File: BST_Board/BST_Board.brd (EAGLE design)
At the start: 59.4 x 27.9 mm, 35 parts, among them J1 UP2-AH-1-TH, J4 EMPCB.SMAFSTJ.B.HT, U1 STM32L053C8T6, U2 RFM69HCW, U5 LM3671MF-3.3/NOPB, Y1 ECS-80-S-4X

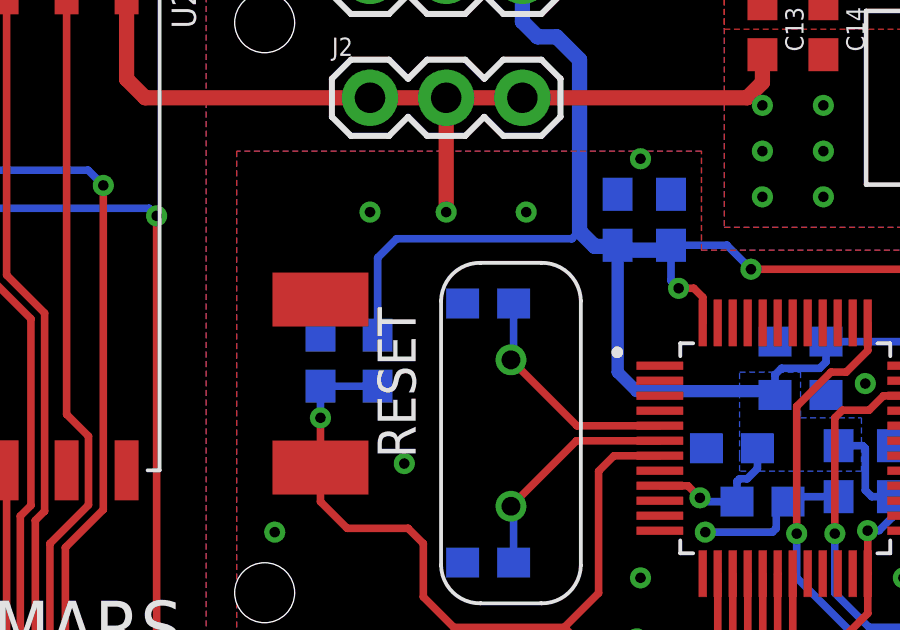
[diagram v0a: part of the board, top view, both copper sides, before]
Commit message: Fixed reset circuit
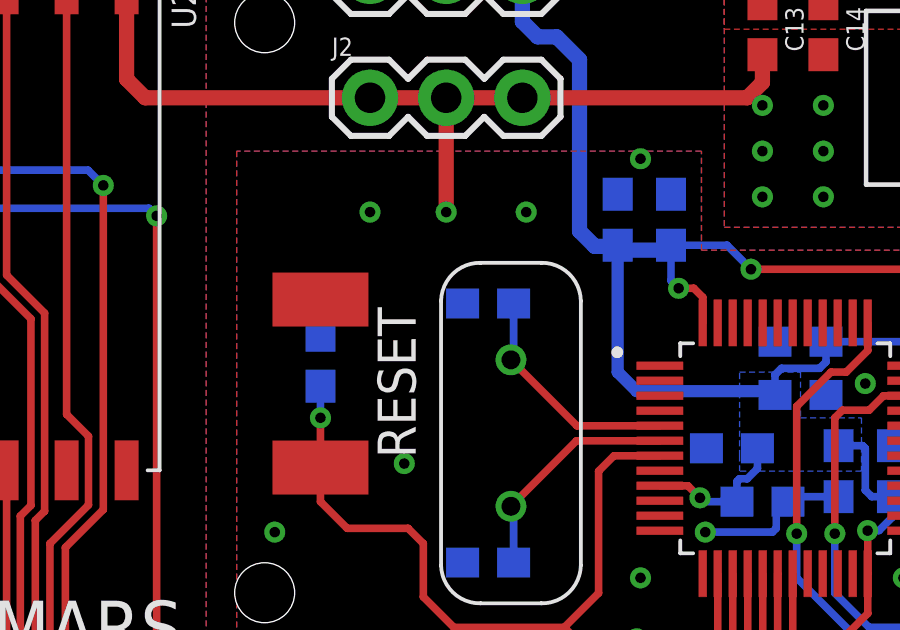
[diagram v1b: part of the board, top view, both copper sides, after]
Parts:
- removed R5: 1k, SparkFun-Resistors:0603
- C17: value 4.7uF -> 0.1uF
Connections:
- net 3.3V: no longer R5.2
- net NRST: no longer R5.1
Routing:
- net 3.3V: track 150.9 -> 141.2 mm
- net NRST: track 48.3 -> 46.3 mm
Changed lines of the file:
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@@
 <attribute name="PROD_ID" value="CAP-00868" x="38.862" y="13.97" size="1.778" layer="28" rot="MR0" display="off"/>
 </element>
-<element name="C17" library="SparkFun-Capacitors" library_urn="urn:adsk.eagle:library:510" package="0603" package3d_urn="urn:adsk.eagle:package:37414/1" value="4.7uF" x="22.86" y="13.335" rot="MR90">
+<element name="C17" library="SparkFun-Capacitors" library_urn="urn:adsk.eagle:library:510" package="0603" package3d_urn="urn:adsk.eagle:package:37414/1" value="0.1uF" x="22.86" y="13.335" rot="MR90">
 <attribute name="PROD_ID" value="CAP-08280" x="33.528" y="13.335" size="1.778" layer="28" rot="MR90" display="off"/>
 </element>
 <element name="RESET" library="DiscreteComponents" package="SW_2512" value="" x="22.86" y="12.573" rot="R270"/>
-<element name="R5" library="SparkFun-Resistors" library_urn="urn:adsk.eagle:library:532" package="0603" package3d_urn="urn:adsk.eagle:package:39650/1" value="1k" x="24.765" y="13.335" rot="MR90">
-<attribute name="PROD_ID" value="RES-07856" x="32.131" y="-1.143" size="1.778" layer="28" rot="MR90" display="off"/>
-</element>
 <element name="CR1" library="ESD_Protection" package="SOT23-6L" value="USBLC6-2SC6" x="46.99" y="11.43" smashed="yes">
 <attribute name="BUILT_BY" value="EMA_UL_Team" x="46.99" y="11.43" size="1.778" layer="27" display="off"/>
@@
 <wire x1="33.401" y1="12.319" x2="38.012" y2="12.319" width="0.4064" layer="16"/>
 <wire x1="32.766" y1="12.954" x2="33.401" y2="12.319" width="0.4064" layer="16"/>
-<contactref element="R5" pad="2"/>
-<wire x1="31.496" y1="17.653" x2="31.242" y2="17.399" width="0.254" layer="16"/>
-<wire x1="25.4" y1="17.399" x2="24.765" y2="16.764" width="0.254" layer="16"/>
-<wire x1="24.765" y1="16.764" x2="24.765" y2="14.185" width="0.254" layer="16"/>
-<wire x1="31.242" y1="17.399" x2="25.4" y2="17.399" width="0.254" layer="16"/>
+<wire x1="31.496" y1="17.653" x2="31.242" y2="17.399" width="0" layer="19" extent="1-16"/>
+<wire x1="25.4" y1="17.399" x2="24.765" y2="16.764" width="0" layer="19" extent="1-16"/>
+<wire x1="31.242" y1="17.399" x2="25.4" y2="17.399" width="0" layer="19" extent="1-16"/>
 <wire x1="24.511" y1="26.162" x2="23.378" y2="27.295" width="0.508" layer="16"/>
 <wire x1="5.832" y1="27.295" x2="5.334" y2="26.797" width="0.508" layer="16"/>
@@
 <wire x1="52.009" y1="24.826" x2="51.308" y2="25.527" width="0.4064" layer="1"/>
 <wire x1="51.308" y1="25.527" x2="49.403" y2="25.527" width="0.4064" layer="1"/>
+<wire x1="47.2313" y1="25.0450875" x2="49.022" y2="25.146" width="0" layer="19" extent="1-1"/>
+<wire x1="39.624" y1="25.234" x2="43.942" y2="24.2443" width="0" layer="19" extent="1-1"/>
+<wire x1="37.592" y1="25.234" x2="39.624" y2="25.234" width="0" layer="19" extent="1-1"/>
+<wire x1="37.426" y1="10.414" x2="38.012" y2="12.192" width="0" layer="19" extent="16-16"/>
+<wire x1="40.132" y1="10.502" x2="39.497" y2="13.081" width="0" layer="19" extent="16-16"/>
 </signal>
 <signal name="RST">
@@
 <contactref element="SV2" pad="1"/>
 <contactref element="C17" pad="1"/>
-<contactref element="R5" pad="1"/>
 <contactref element="RESET" pad="2"/>
 <contactref element="U1" pad="7"/>
-<wire x1="24.765" y1="12.485" x2="22.86" y2="12.485" width="0.254" layer="16"/>
 <wire x1="22.86" y1="9.773" x2="22.86" y2="8.636" width="0.254" layer="1"/>
 <wire x1="22.86" y1="8.636" x2="23.749" y2="7.747" width="0.254" layer="1"/>
